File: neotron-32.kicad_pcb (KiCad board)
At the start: 2 copper layers, 166.9 x 140.7 mm, 97 parts, among them J1 Conn_02x06, J10 micro SD Card, J11 Conn_02x13_Top_Bottom, J12 AVR-ISP-6, J13 DE9 Male, J14 DE9 Male, J15 Double-mini-DIN-6, J17 DB15HD_Female, J18 Conn_02x05, J2 Conn_02x06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

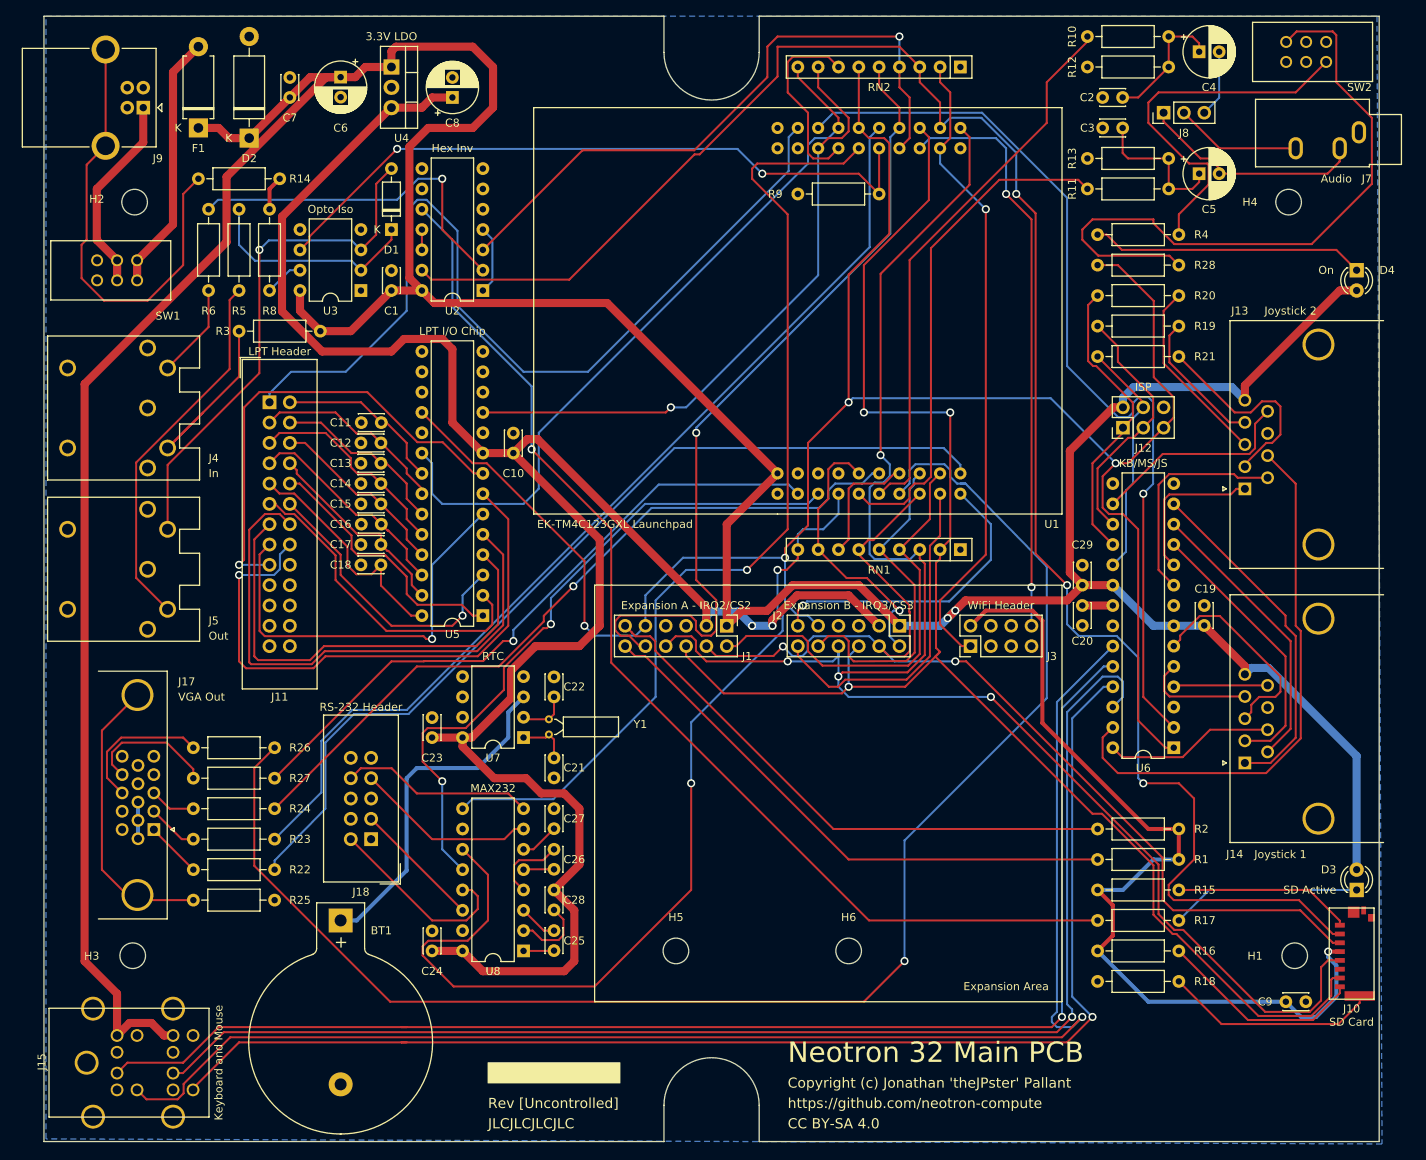
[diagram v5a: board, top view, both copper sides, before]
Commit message: WIP on 4 layer.
It's much easier than the two layer board!
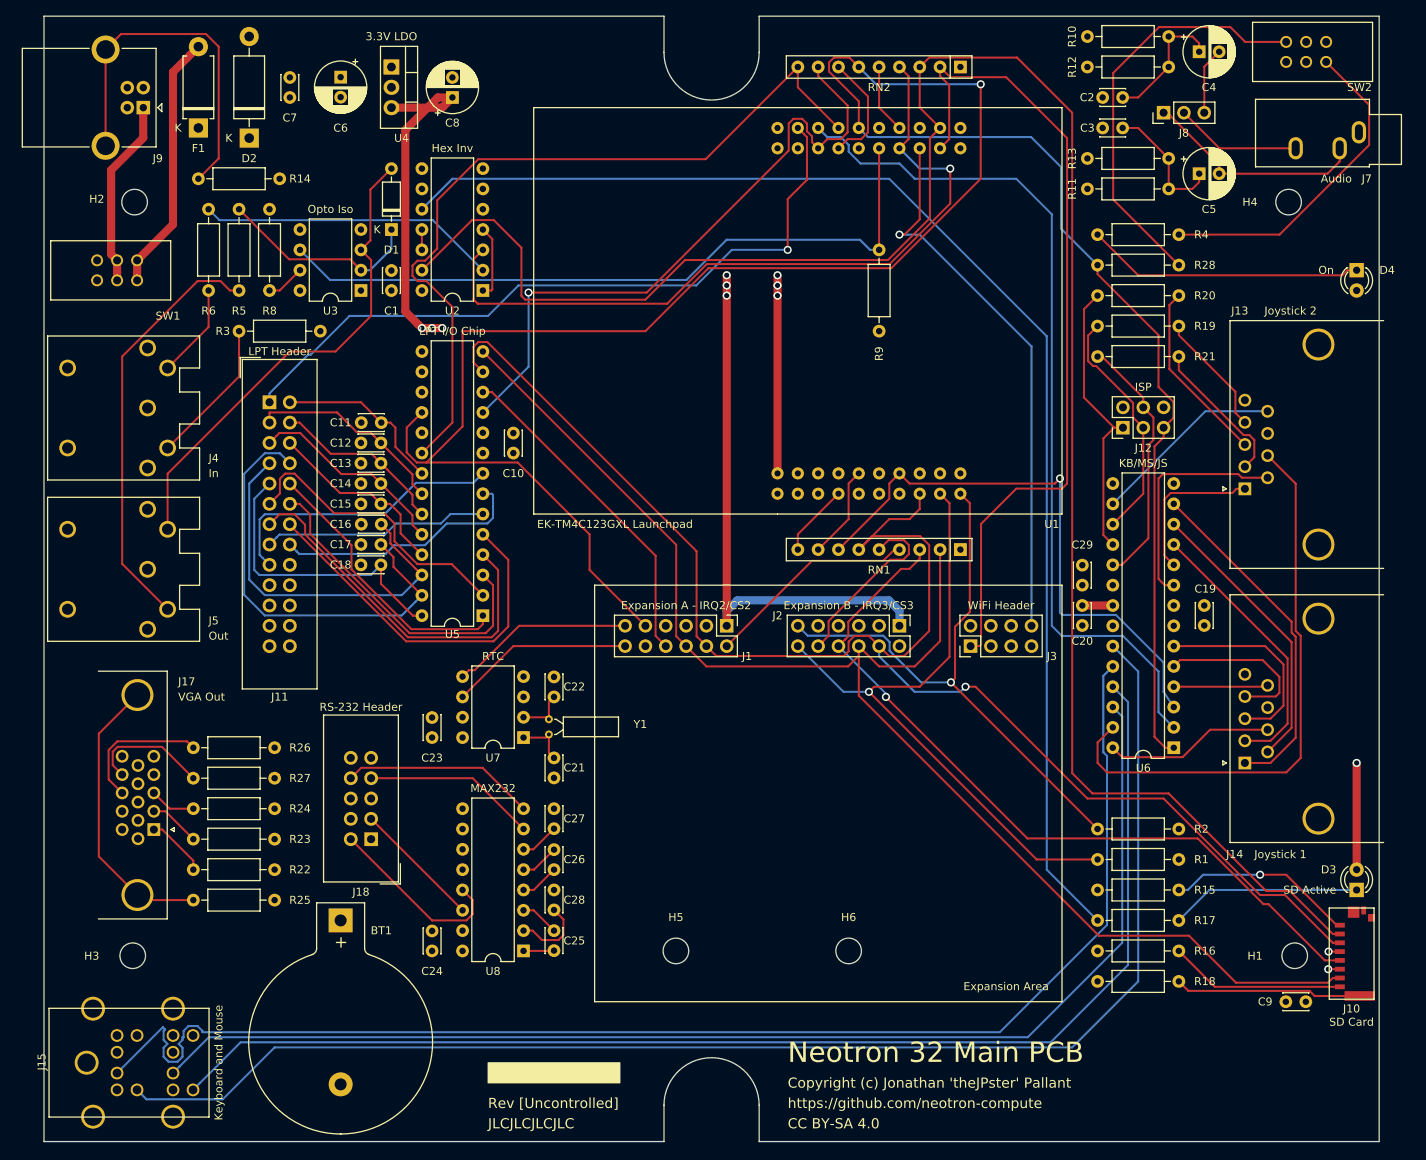
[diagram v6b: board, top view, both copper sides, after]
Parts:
- moved R9 6.98 mm to (175.3, 47.0), turned to 270 degrees
- moved C26 2.54 mm to (134.6, 124.5), turned to 90 degrees
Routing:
- net +5V: track 497.2 -> 136.7 mm, vias 2 -> 7
- net +3V3: track 372.4 -> 45.3 mm, vias 3 -> 4
- net /PB4_VGA_HSYNC: track 190.3 -> 0.00 mm, vias 1 -> 0
- net /PB7_VGA_GREEN: track 124.2 -> 0.00 mm
- net /PC5_U1CTS: track 123.5 -> 0.00 mm, vias 1 -> 0
- net /PF1_VGA_RED: track 115.0 -> 0.00 mm
- net /PB1_U1TX: track 120.9 -> 9.09 mm, vias 2 -> 0
- net /~PB6_SPI_CS2: track 103.7 -> 8.67 mm, vias 1 -> 0
- net /PD3_VGA_BLUE: track 94.0 -> 0.00 mm, vias 1 -> 0
- net /PB0_U1RX: track 84.5 -> 0.00 mm, vias 2 -> 0
- net /PB5_VGA_VSYNC: track 81.9 -> 0.00 mm, vias 1 -> 0
- net /PA2_SPI_CLK: track 211.8 -> 138.2 mm, vias 4 -> 1
- net /PE5_AUDIO_R: track 69.0 -> 0.00 mm
- net /PE4_AUDIO_L: track 63.8 -> 0.00 mm
- net /PA5_SPI_MOSI: track 131.8 -> 193.9 mm, vias 2 -> 1
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- added copper zone on Vcc.Cu, net +3V3
- added copper zone on Vcc.Cu, net +5V
- added copper zone on Gnd.Cu, net GND
- removed copper zone on B.Cu, net GND
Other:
- copper layers 2 -> 4

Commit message: Completed tracking. Just needs a tidy.
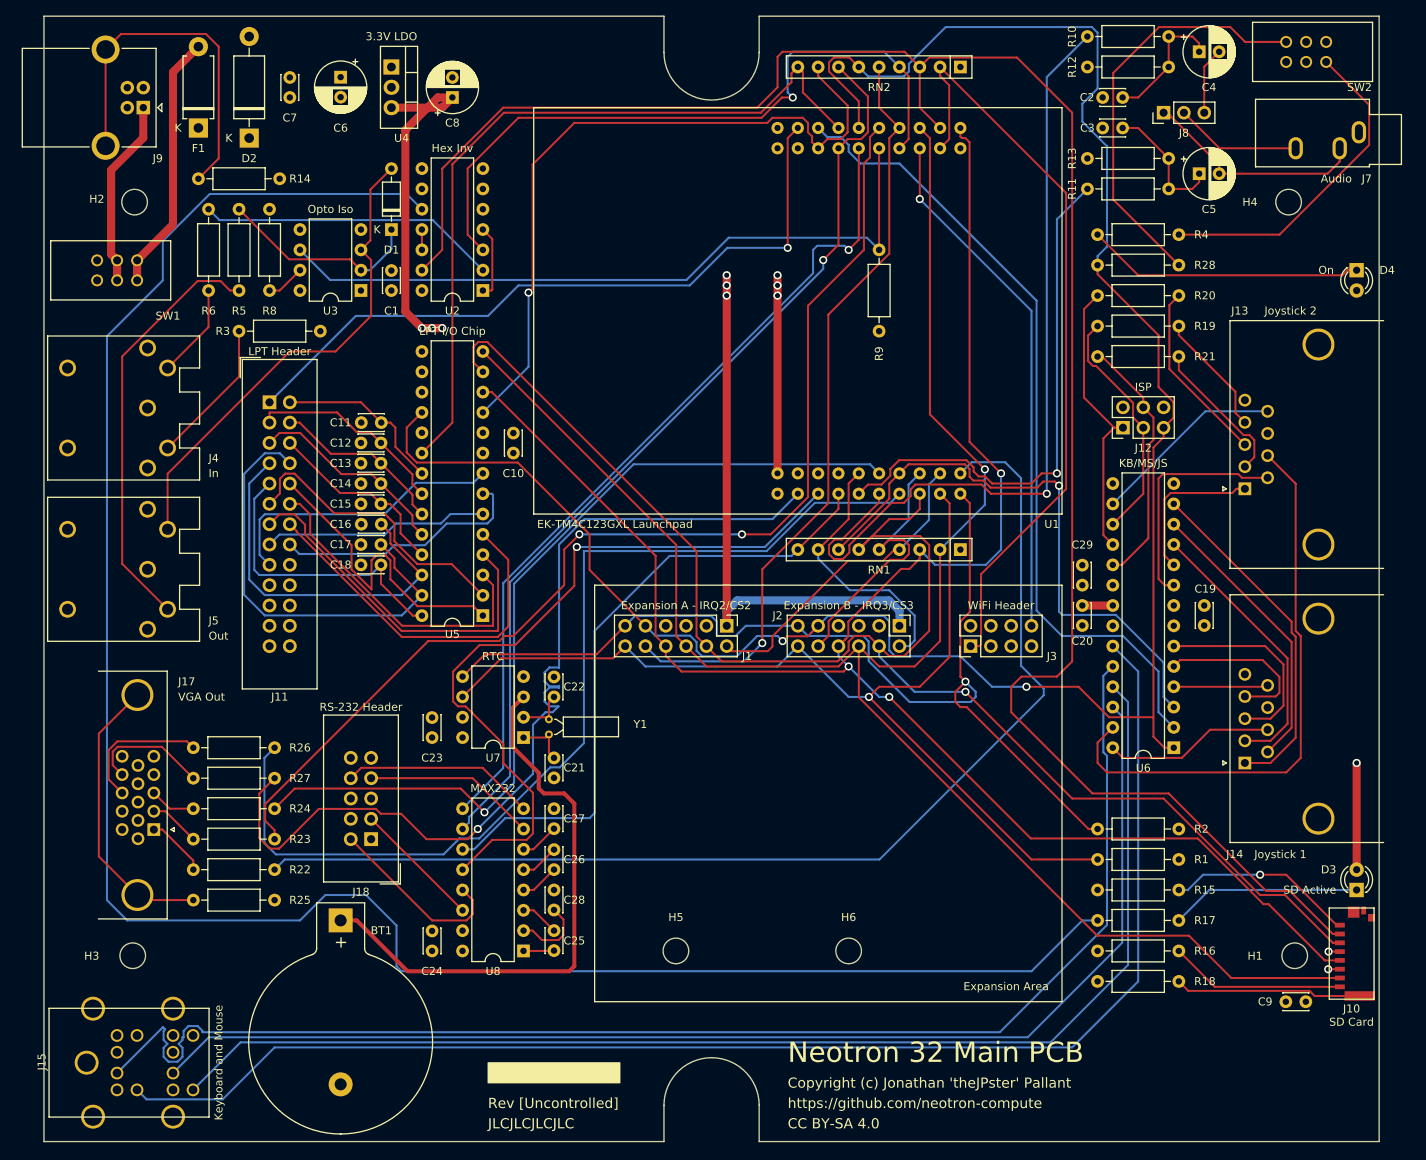
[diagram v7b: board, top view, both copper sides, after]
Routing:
- net /PF1_VGA_RED: track 0.00 -> 142.5 mm
- net /PB7_VGA_GREEN: track 0.00 -> 141.0 mm, vias 0 -> 2
- net /PB4_VGA_HSYNC: track 0.00 -> 125.1 mm
- net /PB5_VGA_VSYNC: track 0.00 -> 119.0 mm, vias 0 -> 1
- net /PD3_VGA_BLUE: track 0.00 -> 110.9 mm, vias 0 -> 1
- net /PC5_U1CTS: track 0.00 -> 106.1 mm, vias 0 -> 1
- net /PC4_U1RTS: track 14.2 -> 118.8 mm, vias 0 -> 1
- net /PE5_AUDIO_R: track 0.00 -> 102.8 mm, vias 0 -> 1
- net Net-(R17-Pad2): track 163.5 -> 256.6 mm
- net /PB0_U1RX: track 0.00 -> 93.1 mm, vias 0 -> 1
- net /PA2_SPI_CLK: track 138.2 -> 230.7 mm, vias 1 -> 3
- net /~PB6_SPI_CS2: track 8.67 -> 96.5 mm, vias 0 -> 1
- net +BATT: track 0.00 -> 71.0 mm
- net /PB1_U1TX: track 9.09 -> 79.9 mm
- net /PE4_AUDIO_L: track 0.00 -> 66.2 mm, vias 0 -> 1
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
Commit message: Tidied up layout a bit. Also ensured all four layers in release.sh.
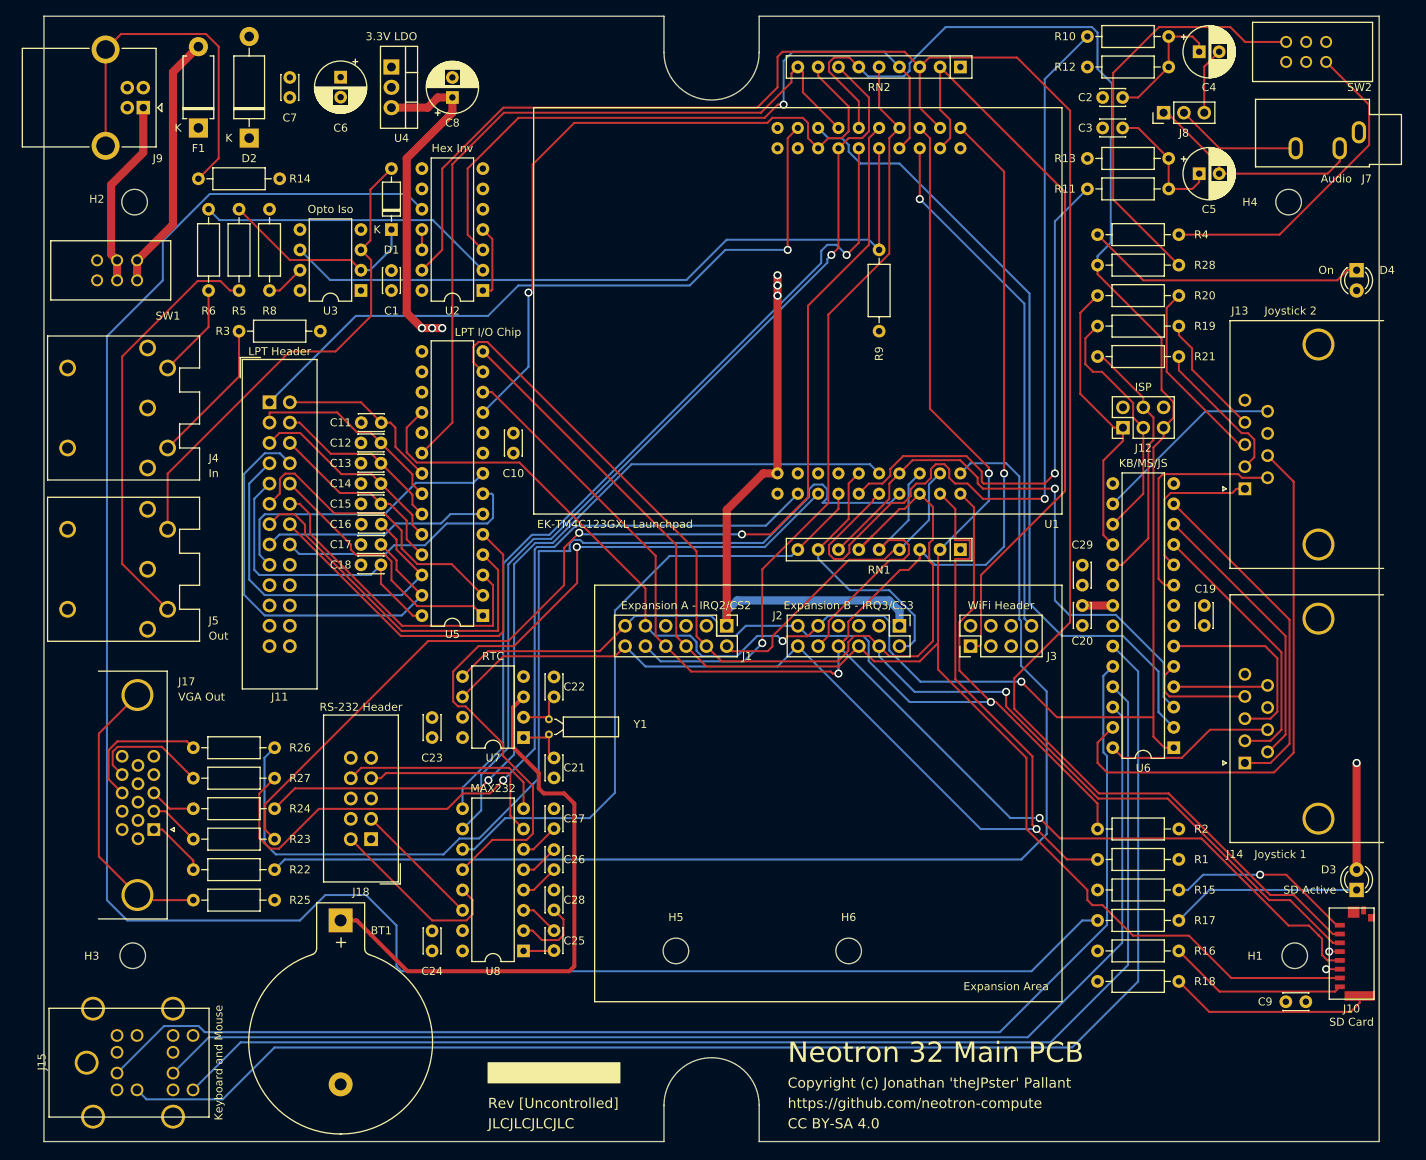
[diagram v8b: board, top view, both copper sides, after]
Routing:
- net +5V: track 136.7 -> 115.6 mm, vias 7 -> 4
- net /PA6_I2C_SCL: track 128.2 -> 145.6 mm
- net /PF1_VGA_RED: track 142.5 -> 153.1 mm
- net /PB5_VGA_VSYNC: track 119.0 -> 109.1 mm
- net /Keyboard, Mouse and Joystick/KB_DAT: track 173.7 -> 165.0 mm
- net /PB4_VGA_HSYNC: track 125.1 -> 133.0 mm
- net /Parallel Printer/ACK: track 39.8 -> 32.7 mm
- net /Keyboard, Mouse and Joystick/RIGHT_GND_JS1: track 20.9 -> 13.9 mm
- net /PA4_SPI_MISO: track 234.5 -> 228.7 mm
- net /PE5_AUDIO_R: track 102.8 -> 106.4 mm
- net /~PA3_SPI_CS0: track 246.8 -> 243.2 mm
- net /RS-232 Serial Port/RS232_RTS_OUT: track 21.7 -> 25.2 mm
- net /PD3_VGA_BLUE: track 110.9 -> 107.8 mm
- net Net-(J10-Pad9): track 23.4 -> 25.5 mm
- net /PA7_I2C_SDA: track 130.1 -> 128.1 mm
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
